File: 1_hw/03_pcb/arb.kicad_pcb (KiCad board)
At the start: 4 copper layers, 100 x 100 mm, 0 parts

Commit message: FEAT: Initial board placement started.
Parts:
- added C1: 1u, Capacitor_SMD:C_0603_1608Metric, F.Cu at (-92.1, 105.8)
- added C10: 2.2u, Capacitor_SMD:C_0603_1608Metric, F.Cu at (-92.1, 128.4)
- added C100: 100n, Capacitor_SMD:C_0603_1608Metric, F.Cu at (126.6, 109.2)
- added C101: 100n, Capacitor_SMD:C_0603_1608Metric, F.Cu at (137.9, 108.7)
- added C102: 100n, Capacitor_SMD:C_0603_1608Metric, F.Cu at (245.0, 110.6)
- added C103: 100n, Capacitor_SMD:C_0603_1608Metric, F.Cu at (252.0, 106.0)
- added C104: 100n, Capacitor_SMD:C_0603_1608Metric, F.Cu at (254.5, 116.7)
- added C105: 5p, Capacitor_SMD:C_0603_1608Metric, F.Cu at (251.0, 131.0)
- added C106: 100n, Capacitor_SMD:C_0603_1608Metric, F.Cu at (269.0, 111.0)
- added C107: 100n, Capacitor_SMD:C_0603_1608Metric, F.Cu at (269.0, 112.5)
- added C108: 5p, Capacitor_SMD:C_0603_1608Metric, F.Cu at (256.0, 128.5)
- added C109: 22p, Capacitor_SMD:C_0603_1608Metric, F.Cu at (225.4, 149.9)
- added C11: 1u, Capacitor_SMD:C_0603_1608Metric, F.Cu at (-92.1, 130.9)
- added C110: 100n, Capacitor_SMD:C_0603_1608Metric, F.Cu at (59.0, 158.4)
- added C111: 100n, Capacitor_SMD:C_0603_1608Metric, F.Cu at (50.0, 163.7)
- added C112: 100n, Capacitor_SMD:C_0603_1608Metric, F.Cu at (75.2, 158.4)
- added C113: 100n, Capacitor_SMD:C_0603_1608Metric, F.Cu at (63.0, 158.4)
- added C12: 1u, Capacitor_SMD:C_0603_1608Metric, F.Cu at (-88.1, 105.8)
- added C13: 2.2u, Capacitor_SMD:C_0603_1608Metric, F.Cu at (-88.1, 108.3)
- added C14: 2.2u, Capacitor_SMD:C_0603_1608Metric, F.Cu at (-88.1, 110.8)
- added C15: 4.7u, Capacitor_SMD:C_0603_1608Metric, F.Cu at (-88.1, 113.3)
- added C16: 100n, Capacitor_SMD:C_0603_1608Metric, F.Cu at (-88.1, 115.8)
- added C17: 10n, Capacitor_SMD:C_0603_1608Metric, F.Cu at (-88.1, 118.3)
- added C18: 4.7n, Capacitor_SMD:C_0603_1608Metric, F.Cu at (-88.1, 120.8)
- added C19: 6.8p, Capacitor_SMD:C_0603_1608Metric, F.Cu at (-88.1, 123.3)
- added C2: 1u, Capacitor_SMD:C_0603_1608Metric, F.Cu at (-92.1, 108.3)
- added C20: 220n, Capacitor_SMD:C_0603_1608Metric, F.Cu at (-88.1, 125.8)
- added C21: 6.8p, Capacitor_SMD:C_0603_1608Metric, F.Cu at (-88.1, 128.4)
- added C22: 4.7u, Capacitor_SMD:C_0603_1608Metric, F.Cu at (-88.1, 130.9)
- added C23: 4.7u, Capacitor_SMD:C_0603_1608Metric, F.Cu at (-84.1, 105.8)
- added C24: 4.7u, Capacitor_SMD:C_0603_1608Metric, F.Cu at (-84.1, 108.3)
- added C25: 4.7u, Capacitor_SMD:C_0603_1608Metric, F.Cu at (-84.1, 110.8)
- added C26: 4.7u, Capacitor_SMD:C_0603_1608Metric, F.Cu at (-84.1, 113.3)
- added C27: 4.7u, Capacitor_SMD:C_0603_1608Metric, F.Cu at (-84.1, 115.8)
- added C28: 100n, Capacitor_SMD:C_0603_1608Metric, F.Cu at (-84.1, 118.3)
- added C29: 4.7u, Capacitor_SMD:C_0603_1608Metric, F.Cu at (-84.1, 120.8)
- added C3: 1u, Capacitor_SMD:C_0603_1608Metric, F.Cu at (-92.1, 110.8)
- added C30: 4.7u, Capacitor_SMD:C_0603_1608Metric, F.Cu at (-84.1, 123.3)
- added C31: 100n, Capacitor_SMD:C_0603_1608Metric, F.Cu at (-84.1, 125.8)
- added C32: 100n, Capacitor_SMD:C_0603_1608Metric, F.Cu at (-84.1, 128.4)
- added C33: 100n, Capacitor_SMD:C_0603_1608Metric, F.Cu at (187.8, 50.0)
- added C34: 100n, Capacitor_SMD:C_0603_1608Metric, F.Cu at (193.9, 88.0)
- added C35: 100n, Capacitor_SMD:C_0603_1608Metric, F.Cu at (186.0, 66.0)
- added C36: 100n, Capacitor_SMD:C_0603_1608Metric, F.Cu at (171.0, 57.5)
- added C37: 5p, Capacitor_SMD:C_0603_1608Metric, F.Cu at (185.5, 71.6)
- added C38: 2.2u, Capacitor_SMD:C_0603_1608Metric, F.Cu at (-35.8, 282.7)
- added C39: 2.2u, Capacitor_SMD:C_0603_1608Metric, F.Cu at (-35.8, 285.2)
- added C4: 10u, Capacitor_SMD:C_0603_1608Metric, F.Cu at (-92.1, 113.3)
- added C40: 100n, Capacitor_SMD:C_0603_1608Metric, F.Cu at (-35.8, 287.7)
- added C41: 100n, Capacitor_SMD:C_0603_1608Metric, F.Cu at (-35.8, 290.2)
- added C42: 10u, Capacitor_SMD:C_0603_1608Metric, F.Cu at (-35.8, 292.7)
- added C43: 15p, Capacitor_SMD:C_0603_1608Metric, F.Cu at (142.5, 76.8)
- added C44: 100n, Capacitor_SMD:C_0603_1608Metric, F.Cu at (-31.8, 282.7)
- added C45: 15p, Capacitor_SMD:C_0603_1608Metric, F.Cu at (142.5, 74.2)
- added C46: 100n, Capacitor_SMD:C_0603_1608Metric, F.Cu at (-31.8, 287.7)
- added C47: 100n, Capacitor_SMD:C_0603_1608Metric, F.Cu at (-31.8, 290.2)
- added C48: 100n, Capacitor_SMD:C_0603_1608Metric, F.Cu at (-31.8, 292.7)
- added C49: 1u, Capacitor_SMD:C_0603_1608Metric, F.Cu at (-31.8, 295.2)
- added C5: 4.7u, Capacitor_SMD:C_0603_1608Metric, F.Cu at (-92.1, 115.8)
- added C50: 100n, Capacitor_SMD:C_0603_1608Metric, F.Cu at (-27.8, 282.7)
- added C51: 100n, Capacitor_SMD:C_0603_1608Metric, F.Cu at (-27.8, 285.2)
- added C52: 100n, Capacitor_SMD:C_0603_1608Metric, F.Cu at (-27.8, 287.7)
- added C53: 1u, Capacitor_SMD:C_0603_1608Metric, F.Cu at (-27.8, 290.2)
- added C54: 100n, Capacitor_SMD:C_0603_1608Metric, F.Cu at (-27.8, 292.7)
- added C55: 100n, Capacitor_SMD:C_0603_1608Metric, F.Cu at (-27.8, 295.2)
- added C56: 100n, Capacitor_SMD:C_0603_1608Metric, F.Cu at (-23.8, 282.7)
- added C57: 100n, Capacitor_SMD:C_0603_1608Metric, F.Cu at (-23.8, 285.2)
- added C58: 100n, Capacitor_SMD:C_0603_1608Metric, F.Cu at (-23.8, 287.7)
- added C59: 100n, Capacitor_SMD:C_0603_1608Metric, F.Cu at (116.0, 103.8)
- added C6: 100n, Capacitor_SMD:C_0603_1608Metric, F.Cu at (-92.1, 118.3)
- added C60: 100n, Capacitor_SMD:C_0603_1608Metric, F.Cu at (108.5, 99.3)
- added C61: 4.7u, Capacitor_SMD:C_0603_1608Metric, F.Cu at (117.5, 103.8)
- added C62: 4.7u, Capacitor_SMD:C_0603_1608Metric, F.Cu at (108.5, 97.8)
- added C63: 4.7u, Capacitor_SMD:C_0603_1608Metric, F.Cu at (108.5, 102.8)
- added C64: 100n, Capacitor_SMD:C_0603_1608Metric, F.Cu at (108.5, 101.3)
- added C65: 100n, Capacitor_SMD:C_0603_1608Metric, F.Cu at (119.0, 92.8)
- added C66: 100n, Capacitor_SMD:C_0603_1608Metric, F.Cu at (116.5, 92.0)
- added C67: 100n, Capacitor_SMD:C_0603_1608Metric, F.Cu at (112.5, 103.8)
- added C68: 4.7u, Capacitor_SMD:C_0603_1608Metric, F.Cu at (119.0, 91.3)
- added C69: 4.7u, Capacitor_SMD:C_0603_1608Metric, F.Cu at (115.0, 92.0)
- added C7: 1u, Capacitor_SMD:C_0603_1608Metric, F.Cu at (-92.1, 120.8)
- added C70: 4.7u, Capacitor_SMD:C_0603_1608Metric, F.Cu at (114.0, 103.8)
- added C71: 100n, Capacitor_SMD:C_0603_1608Metric, F.Cu at (132.1, 58.6)
- added C72: 4.7u, Capacitor_SMD:C_0603_1608Metric, F.Cu at (117.1, 74.3)
- added C73: 27p, Capacitor_SMD:C_0603_1608Metric, F.Cu at (113.1, 70.1)
- added C74: 4.7u, Capacitor_SMD:C_0603_1608Metric, F.Cu at (117.1, 77.8)
- added C75: 27p, Capacitor_SMD:C_0603_1608Metric, F.Cu at (116.4, 67.3)
- added C76: 100n, Capacitor_SMD:C_0603_1608Metric, F.Cu at (118.6, 74.3)
- added C77: 3.3u, Capacitor_SMD:C_0603_1608Metric, F.Cu at (133.6, 69.6)
- added C78: 100n, Capacitor_SMD:C_0603_1608Metric, F.Cu at (118.6, 77.8)
- added C79: 100n, Capacitor_SMD:C_0603_1608Metric, F.Cu at (117.8, 80.1)
- added C8: 2.2u, Capacitor_SMD:C_0603_1608Metric, F.Cu at (-92.1, 123.3)
- added C80: 100n, Capacitor_SMD:C_0603_1608Metric, F.Cu at (136.1, 78.1)
- added C81: 100n, Capacitor_SMD:C_0603_1608Metric, F.Cu at (123.1, 67.6)
- added C82: 100n, Capacitor_SMD:C_0603_1608Metric, F.Cu at (125.4, 84.3)
- added C83: 100n, Capacitor_SMD:C_0603_1608Metric, F.Cu at (131.6, 84.6)
- added C84: 100n, Capacitor_SMD:C_0603_1608Metric, F.Cu at (136.1, 74.6)
- added C85: 100n, Capacitor_SMD:C_0603_1608Metric, F.Cu at (128.1, 67.6)
- added C86: 100n, Capacitor_SMD:C_0603_1608Metric, F.Cu at (155.9, 57.6)
- added C87: 100n, Capacitor_SMD:C_0603_1608Metric, F.Cu at (187.5, 78.4)
- added C88: 100n, Capacitor_SMD:C_0603_1608Metric, F.Cu at (189.5, 104.0)
- added C89: 100n, Capacitor_SMD:C_0603_1608Metric, F.Cu at (189.5, 107.0)
- added C9: 2.2u, Capacitor_SMD:C_0603_1608Metric, F.Cu at (-92.1, 125.8)
- added C90: 100n, Capacitor_SMD:C_0603_1608Metric, F.Cu at (176.0, 107.0)
- added C91: 100n, Capacitor_SMD:C_0603_1608Metric, F.Cu at (116.9, 121.9)
- added C92: 100n, Capacitor_SMD:C_0603_1608Metric, F.Cu at (111.9, 121.9)
- added C93: 100n, Capacitor_SMD:C_0603_1608Metric, F.Cu at (119.4, 121.9)
- added C94: 5p, Capacitor_SMD:C_0603_1608Metric, F.Cu at (131.3, 117.3)
- added C95: 5p, Capacitor_SMD:C_0603_1608Metric, F.Cu at (168.0, 104.7)
- added C96: 100n, Capacitor_SMD:C_0603_1608Metric, F.Cu at (149.6, 115.9)
- added C97: 100n, Capacitor_SMD:C_0603_1608Metric, F.Cu at (148.6, 106.0)
- added C98: 100n, Capacitor_SMD:C_0603_1608Metric, F.Cu at (138.8, 119.9)
- added C99: 100n, Capacitor_SMD:C_0603_1608Metric, F.Cu at (155.6, 101.5)
- added D1: LED, LED_SMD:LED_1206_3216Metric, F.Cu at (-66.1, 120.9)
- added D2: MBRM120ET1G, BRZK_DIODE:D_SMP_DO-216AA, F.Cu at (-66.1, 106.6)
- added D3: MBRM120ET1G, BRZK_DIODE:D_SMP_DO-216AA, F.Cu at (-66.1, 110.8)
- added D4: LED, LED_SMD:LED_1206_3216Metric, F.Cu at (79.0, 94.1)
- added D5: LED, LED_SMD:LED_1206_3216Metric, F.Cu at (83.5, 94.1)
- added D6: LED, LED_SMD:LED_1206_3216Metric, F.Cu at (88.0, 94.1)
- added D7: LED, LED_SMD:LED_1206_3216Metric, F.Cu at (104.0, 76.1)
- added D8: LED, LED_SMD:LED_1206_3216Metric, F.Cu at (108.5, 76.0)
- added D9: BAT54L, Package_TO_SOT_SMD:SOT-23, F.Cu at (260.1, 130.1)
- added FB1: 100@100MHz, Inductor_SMD:L_0603_1608Metric, F.Cu at (187.8, 47.0)
- added FB2: 30@100MHz, Inductor_SMD:L_0603_1608Metric, F.Cu at (193.9, 86.0)
- added H1: MOUNTING HOLE, MountingHole:MountingHole_3.2mm_M3_Pad, F.Cu at (105.7, 48.0)
- added H2: MOUNTING HOLE, MountingHole:MountingHole_3.2mm_M3_Pad, F.Cu at (195.7, 48.0)
- added H3: MOUNTING HOLE, MountingHole:MountingHole_3.2mm_M3_Pad, F.Cu at (105.7, 137.9)
- added H4: MOUNTING HOLE, MountingHole:MountingHole_3.2mm_M3_Pad, F.Cu at (195.7, 137.9)
- added J1: TYPE-C-31-M-12, Connector_USB:USB_C_Receptacle_GCT_USB4105-xx-A_16P_TopMnt_Horizontal, F.Cu at (104.5, 64.0)
- added J2: SMA, BRZK_CONN_COAX:SMA_TH_Horizontal_KH-SMA-K513-G, F.Cu at (196.2, 61.1)
- added J3: SMA, BRZK_CONN_COAX:SMA_TH_Horizontal_KH-SMA-K513-G, F.Cu at (196.2, 70.8)
- added J4: BNC, BRZK_CONN_COAX:BNC_TH_Horizontal_DOSIN-801-0050, F.Cu at (151.8, 136.2)
- added J5: PH-00244, Connector_PinHeader_2.54mm:PinHeader_2x05_P2.54mm_Vertical, F.Cu at (-67.7, 82.3)
- added L1: 4.7u, Inductor_SMD:L_0603_1608Metric, F.Cu at (-84.1, 130.9)
- added L2: 4.7u, Inductor_SMD:L_0603_1608Metric, F.Cu at (-80.1, 105.8)
- added L3: 10u, Inductor_SMD:L_0603_1608Metric, F.Cu at (114.9, 73.6)
- added L4: 10u, Inductor_SMD:L_0603_1608Metric, F.Cu at (114.8, 77.1)
- added R1: 10k, Resistor_SMD:R_0603_1608Metric, F.Cu at (-80.1, 108.3)
- added R10: 84.5k, Resistor_SMD:R_0603_1608Metric, F.Cu at (-80.1, 130.9)
- added R11: 0, Resistor_SMD:R_0603_1608Metric, F.Cu at (-76.1, 105.8)
- added R12: 0, Resistor_SMD:R_0603_1608Metric, F.Cu at (-76.1, 108.3)
- added R13: 104k, Resistor_SMD:R_0603_1608Metric, F.Cu at (-76.1, 110.8)
- added R14: 1.30M, Resistor_SMD:R_0603_1608Metric, F.Cu at (-76.1, 113.3)
- added R15: 0, Resistor_SMD:R_0603_1608Metric, F.Cu at (-76.1, 115.8)
- added R16: 0, Resistor_SMD:R_0603_1608Metric, F.Cu at (-76.1, 118.3)
- added R17: 0, Resistor_SMD:R_0603_1608Metric, F.Cu at (-76.1, 120.8)
- added R18: 0, Resistor_SMD:R_0603_1608Metric, F.Cu at (-76.1, 123.3)
- added R19: 10k, Resistor_SMD:R_0603_1608Metric, F.Cu at (185.2, 49.3)
- added R2: 10k, Resistor_SMD:R_0603_1608Metric, F.Cu at (-80.1, 110.8)
- added R20: 24.9, Resistor_SMD:R_0603_1608Metric, F.Cu at (186.1, 55.5)
- added R21: 10k, Resistor_SMD:R_0603_1608Metric, F.Cu at (192.3, 84.0)
- added R22: 24.9, Resistor_SMD:R_0603_1608Metric, F.Cu at (193.2, 95.0)
- added R23: 10k, Resistor_SMD:R_0603_1608Metric, F.Cu at (184.5, 66.0)
- added R24: 10k, Resistor_SMD:R_0603_1608Metric, F.Cu at (183.0, 60.0)
- added R25: 10k, Resistor_SMD:R_0603_1608Metric, F.Cu at (182.2, 57.5)
- added R26: 100, Resistor_SMD:R_0603_1608Metric, F.Cu at (187.0, 70.0)
- added R27: 100, Resistor_SMD:R_0603_1608Metric, F.Cu at (188.5, 71.6)
- added R28: 24.9, Resistor_SMD:R_0603_1608Metric, F.Cu at (182.2, 56.0)
- added R29: 24.9, Resistor_SMD:R_0603_1608Metric, F.Cu at (173.0, 60.0)
- added R3: 10k, Resistor_SMD:R_0603_1608Metric, F.Cu at (-80.1, 113.3)
- added R30: 0, Resistor_SMD:R_0603_1608Metric, F.Cu at (171.0, 56.0)
- added R31: 10k, Resistor_SMD:R_0603_1608Metric, F.Cu at (-23.8, 290.2)
- added R32: 10k, Resistor_SMD:R_0603_1608Metric, F.Cu at (138.4, 53.1)
- added R33: 10k, Resistor_SMD:R_0603_1608Metric, F.Cu at (126.2, 53.1)
- added R34: 10k, Resistor_SMD:R_0603_1608Metric, F.Cu at (113.8, 87.1)
- added R35: 10k, Resistor_SMD:R_0603_1608Metric, F.Cu at (110.8, 87.1)
- added R36: 10k, Resistor_SMD:R_0603_1608Metric, F.Cu at (103.3, 95.8)
- added R37: 220, Resistor_SMD:R_0603_1608Metric, F.Cu at (79.0, 90.1)
- added R38: 220, Resistor_SMD:R_0603_1608Metric, F.Cu at (83.5, 90.1)
- added R39: 220, Resistor_SMD:R_0603_1608Metric, F.Cu at (88.0, 90.1)
- added R4: 499, Resistor_SMD:R_0603_1608Metric, F.Cu at (-80.1, 115.8)
- added R40: 100, Resistor_SMD:R_0603_1608Metric, F.Cu at (110.1, 104.8)
- added R41: 1k, Resistor_SMD:R_0603_1608Metric, F.Cu at (113.6, 83.1)
- added R42: 10k, Resistor_SMD:R_0603_1608Metric, F.Cu at (122.8, 60.1)
- added R43: 2.05k, Resistor_SMD:R_0603_1608Metric, F.Cu at (123.6, 62.6)
- added R44: 10k, Resistor_SMD:R_0603_1608Metric, F.Cu at (132.1, 60.1)
- added R45: 10k, Resistor_SMD:R_0603_1608Metric, F.Cu at (132.1, 61.6)
- added R46: 12k, Resistor_SMD:R_0603_1608Metric, F.Cu at (119.5, 67.5)
- added R47: 4.7k, Resistor_SMD:R_0603_1608Metric, F.Cu at (116.1, 63.6)
- added R48: 10k, Resistor_SMD:R_0603_1608Metric, F.Cu at (119.1, 63.6)
- added R49: 0, Resistor_SMD:R_0603_1608Metric, F.Cu at (118.6, 84.1)
- added R5: 110k, Resistor_SMD:R_0603_1608Metric, F.Cu at (-80.1, 118.3)
- added R50: 0, Resistor_SMD:R_0603_1608Metric, F.Cu at (121.6, 84.1)
- added R51: 220, Resistor_SMD:R_0603_1608Metric, F.Cu at (104.0, 72.1)
- added R52: 220, Resistor_SMD:R_0603_1608Metric, F.Cu at (108.5, 72.0)
- added R53: 10k, Resistor_SMD:R_0603_1608Metric, F.Cu at (158.5, 61.1)
- added R54: 10k, Resistor_SMD:R_0603_1608Metric, F.Cu at (190.0, 81.5)
- added R55: 10k, Resistor_SMD:R_0603_1608Metric, F.Cu at (146.0, 58.8)
- added R56: 10k, Resistor_SMD:R_0603_1608Metric, F.Cu at (176.0, 79.4)
- added R57: 3.9k, Resistor_SMD:R_0603_1608Metric, F.Cu at (189.5, 102.5)
- added R58: 2k, Resistor_SMD:R_0603_1608Metric, F.Cu at (113.4, 121.9)
- added R59: 10k, Resistor_SMD:R_0603_1608Metric, F.Cu at (117.9, 126.9)
- added R6: 1M, Resistor_SMD:R_0603_1608Metric, F.Cu at (-80.1, 120.8)
- added R60: 24.9, Resistor_SMD:R_0603_1608Metric, F.Cu at (128.8, 118.9)
- added R61: 24.9, Resistor_SMD:R_0603_1608Metric, F.Cu at (172.0, 106.3)
- added R62: 24.9, Resistor_SMD:R_0603_1608Metric, F.Cu at (128.8, 115.8)
- added R63: 24.9, Resistor_SMD:R_0603_1608Metric, F.Cu at (172.0, 103.1)
- added R64: 226, Resistor_SMD:R_0603_1608Metric, F.Cu at (134.3, 118.1)
- added R65: 226, Resistor_SMD:R_0603_1608Metric, F.Cu at (134.3, 116.6)
- added R66: 226, Resistor_SMD:R_0603_1608Metric, F.Cu at (164.3, 105.5)
- added R67: 226, Resistor_SMD:R_0603_1608Metric, F.Cu at (164.3, 104.0)
- added R68: 499, Resistor_SMD:R_0603_1608Metric, F.Cu at (137.8, 115.8)
- added R69: 1k, Resistor_SMD:R_0603_1608Metric, F.Cu at (160.3, 103.0)
- added R7: 0, Resistor_SMD:R_0603_1608Metric, F.Cu at (-80.1, 123.3)
- added R70: 499, Resistor_SMD:R_0603_1608Metric, F.Cu at (144.3, 122.1)
- added R71: 1k, Resistor_SMD:R_0603_1608Metric, F.Cu at (153.8, 99.0)
- added R72: 0, Resistor_SMD:R_0603_1608Metric, F.Cu at (151.9, 117.7)
- added R73: 0, Resistor_SMD:R_0603_1608Metric, F.Cu at (145.0, 104.5)
- added R74: 10k, Resistor_SMD:R_0603_1608Metric, F.Cu at (140.4, 109.5)
- added R75: 4.7k, Resistor_SMD:R_0603_1608Metric, F.Cu at (249.0, 115.5)
- added R76: 4.7k, Resistor_SMD:R_0603_1608Metric, F.Cu at (247.0, 115.5)
- added R77: 0, Resistor_SMD:R_0603_1608Metric, F.Cu at (252.5, 131.0)
- added R78: 124k, Resistor_SMD:R_0603_1608Metric, F.Cu at (256.0, 130.1)
- added R79: 10k, Resistor_SMD:R_0603_1608Metric, F.Cu at (267.1, 115.5)
- added R8: 0, Resistor_SMD:R_0603_1608Metric, F.Cu at (-80.1, 125.8)
- added R80: 0, Resistor_SMD:R_0603_1608Metric, F.Cu at (263.5, 131.0)
- added R81: 50, Resistor_SMD:R_0603_1608Metric, F.Cu at (229.5, 149.1)
- added R82: 499, Resistor_SMD:R_0603_1608Metric, F.Cu at (45.0, 160.4)
- added R83: 499, Resistor_SMD:R_0603_1608Metric, F.Cu at (45.0, 158.7)
- added R84: 499, Resistor_SMD:R_0603_1608Metric, F.Cu at (47.5, 157.9)
- added R85: 499, Resistor_SMD:R_0603_1608Metric, F.Cu at (53.6, 166.9)
- added R86: 0, Resistor_SMD:R_0603_1608Metric, F.Cu at (59.0, 159.9)
- added R87: 10k, Resistor_SMD:R_0603_1608Metric, F.Cu at (62.5, 153.9)
- added R88: 5.1k, Resistor_SMD:R_0603_1608Metric, F.Cu at (-60.8, 81.2)
- added R89: 5.1k, Resistor_SMD:R_0603_1608Metric, F.Cu at (-60.8, 83.7)
- added R9: 976k, Resistor_SMD:R_0603_1608Metric, F.Cu at (-80.1, 128.4)
- added R90: 0, Resistor_SMD:R_0603_1608Metric, F.Cu at (-60.8, 86.2)
- added R91: 0, Resistor_SMD:R_0603_1608Metric, F.Cu at (-60.8, 88.8)
- added R92: 0, Resistor_SMD:R_0603_1608Metric, F.Cu at (-60.8, 91.3)
- added R93: 0, Resistor_SMD:R_0603_1608Metric, F.Cu at (-56.8, 81.2)
- added R94: 0, Resistor_SMD:R_0603_1608Metric, F.Cu at (-56.8, 83.7)
- added R95: 0, Resistor_SMD:R_0603_1608Metric, F.Cu at (-56.8, 86.2)
- added R96: 0, Resistor_SMD:R_0603_1608Metric, F.Cu at (-56.8, 88.8)
- added R97: 0, Resistor_SMD:R_0603_1608Metric, F.Cu at (-56.8, 91.3)
- added SW1: TS-1187A-B-A-B, BRZK_SW:SW_SPST_BUTTON_TS-1187A-B-A-B, F.Cu at (115.2, 48.2)
- added SW2: SS-12D02-VG4, BRZK_SW:SW_TH_Slide_SPDT_Straight_SS-12D02-VG4, F.Cu at (136.5, 48.5)
- added SW3: SS-12D02-VG4, BRZK_SW:SW_TH_Slide_SPDT_Straight_SS-12D02-VG4, F.Cu at (124.2, 48.5)
- added U1: TLV70333DBV, Package_TO_SOT_SMD:SOT-23-5, F.Cu at (-71.5, 106.9)
- added U10: LMK1C1103PWR, Package_SO:TSSOP-8_4.4x3mm_P0.65mm, F.Cu at (176.5, 57.5)
- added U11: STM32F446ZETx, Package_QFP:LQFP-144_20x20mm_P0.5mm, F.Cu at (160.5, 80.0)
- added U12: ICE40UP5K-SG48ITR, Package_DFN_QFN:QFN-48-1EP_7x7mm_P0.5mm_EP5.6x5.6mm, F.Cu at (114.7, 97.7)
- added U13: 93LC56BT-I_OT, Package_TO_SOT_SMD:SOT-23-6, F.Cu at (127.9, 60.0)
- added U14: FT2232HL, Package_QFP:LQFP-64_10x10mm_P0.5mm, F.Cu at (127.5, 76.0)
- added U15: W25Q128JVSIQ, Package_SO:SOIC-8_5.23x5.23mm_P1.27mm, F.Cu at (151.5, 61.6)
- added U16: W25Q128JVSIQ, Package_SO:SOIC-8_5.23x5.23mm_P1.27mm, F.Cu at (183.0, 82.0)
- added U17: AD9850, Package_SO:SSOP-28_5.3x10.2mm_P0.65mm, F.Cu at (183.0, 106.0)
- added U18: AD9744, Package_SO:TSSOP-28_4.4x9.7mm_P0.65mm, F.Cu at (115.5, 116.5)
- added U19: LM6171, Package_SO:SOIC-8_3.9x4.9mm_P1.27mm, F.Cu at (144.3, 117.1)
- added U2: TLV76133DCY, Package_TO_SOT_SMD:SOT-223-3_TabPin2, F.Cu at (-69.1, 131.8)
- added U20: LM6171, Package_SO:SOIC-8_3.9x4.9mm_P1.27mm, F.Cu at (153.8, 105.0)
- added U21: TMUX6104, Package_SO:TSSOP-14_4.4x5mm_P0.65mm, F.Cu at (132.5, 108.0)
- added U22: TPL0401B-10, Package_TO_SOT_SMD:Texas_R-PDSO-G6, F.Cu at (248.1, 111.8)
- added U23: THS3491, Package_SO:Texas_R-PDSO-G8_EP2.95x4.9mm_Mask2.4x3.1mm, F.Cu at (254.0, 111.4)
- added U24: ADG1219BRJZ, Package_TO_SOT_SMD:SOT-23-8, F.Cu at (265.1, 112.0)
- added U25: LM6171, Package_SO:SOIC-8_3.9x4.9mm_P1.27mm, F.Cu at (53.5, 159.4)
- added U26: TMUX6104, Package_SO:TSSOP-14_4.4x5mm_P0.65mm, F.Cu at (69.5, 158.9)
- added U3: TLV70333DBV, Package_TO_SOT_SMD:SOT-23-5, F.Cu at (-71.5, 111.5)
- added U4: LM3880MF-1AA, Package_TO_SOT_SMD:SOT-23-6, F.Cu at (-71.5, 116.2)
- added U5: TLV70312DBV, Package_TO_SOT_SMD:SOT-23-5, F.Cu at (-71.5, 120.8)
- added U6: TLV70325DBV, Package_TO_SOT_SMD:SOT-23-5, F.Cu at (-71.5, 125.4)
- added U7: TPS65131RGE, Package_DFN_QFN:VQFN-24-1EP_4x4mm_P0.5mm_EP2.45x2.45mm, F.Cu at (-65.8, 116.0)
- added U8: TPD2E001DRL, Package_TO_SOT_SMD:SOT-553, F.Cu at (-67.2, 124.3)
- added U9: ADG1219BRJZ, Package_TO_SOT_SMD:SOT-23-8, F.Cu at (186.5, 62.0)
- added X1: ASE-10.000MHz, Oscillator:Oscillator_SMD_Abracon_ASE-4Pin_3.2x2.5mm, F.Cu at (185.3, 52.0)
- added X2: ASE-100.000MHz, Oscillator:Oscillator_SMD_Abracon_ASE-4Pin_3.2x2.5mm, F.Cu at (192.3, 91.0)
- added Y1: 32.768k, Crystal:Crystal_SMD_3215-2Pin_3.2x1.5mm, F.Cu at (145.5, 75.5)
- added Y2: 12 MHz, Crystal:Crystal_SMD_3225-4Pin_3.2x2.5mm, F.Cu at (113.3, 67.4)
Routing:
- added copper zone on In1.Cu, net GND
- added copper zone on In2.Cu, net GND

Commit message: FEAT: Finished placement of components, switches, etc.
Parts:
- moved C55 302.2 mm to (172.0, 68.5), turned to 90 degrees
- moved C39 299.3 mm to (173.8, 71.5)
- moved C53 294.3 mm to (173.8, 75.8)
- moved C54 290.9 mm to (173.8, 83.0)
- moved C51 289.6 mm to (173.8, 77.2)
- moved C42 288.9 mm to (147.7, 69.5), turned to 180 degrees
- moved C56 285.8 mm to (163.5, 66.7), turned to 90 degrees
- moved C57 284.2 mm to (158.0, 66.7), turned to 90 degrees
- moved R31 283.9 mm to (151.0, 66.5)
- moved C40 282.6 mm to (148.0, 73.0), turned to 90 degrees
- moved C52 280.0 mm to (172.0, 91.5)
- moved C58 279.7 mm to (149.4, 68.0), turned to 180 degrees
- moved C41 279.5 mm to (147.2, 79.0), turned to 180 degrees
- moved C38 278.6 mm to (168.5, 93.3), turned to -90 degrees
- moved C48 276.4 mm to (159.5, 93.3), turned to -90 degrees
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
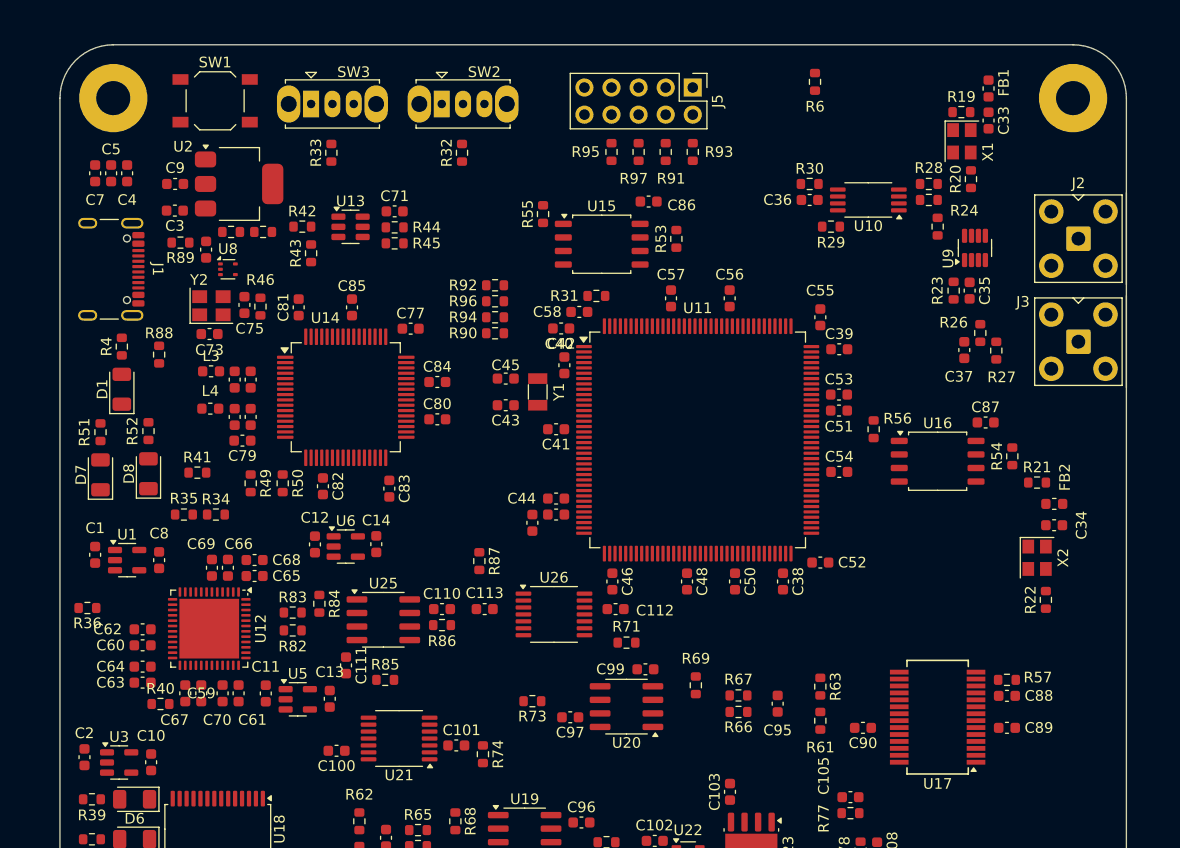
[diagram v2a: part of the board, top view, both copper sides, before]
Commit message: MINOR: Started laying out signal tracks. About 1/4th of the way done. Started on Digital, 3P3V Power, Clocking.
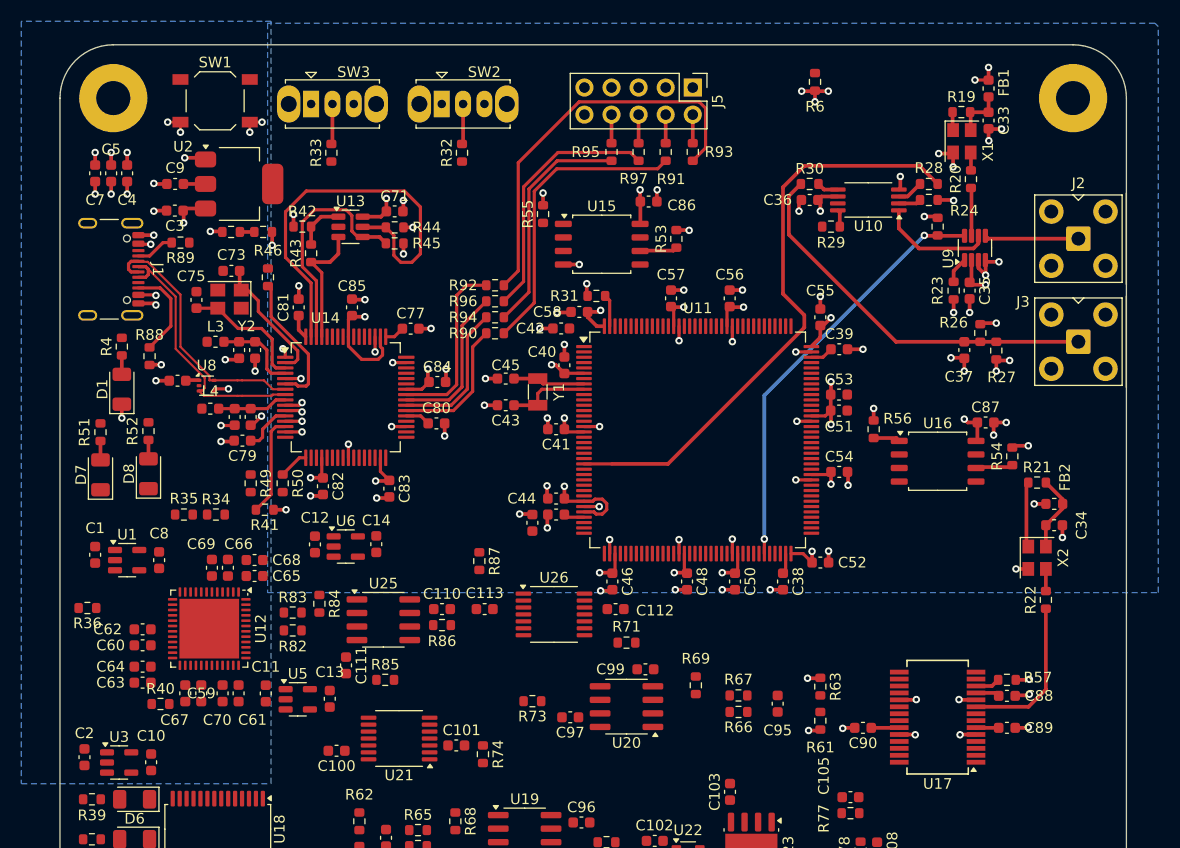
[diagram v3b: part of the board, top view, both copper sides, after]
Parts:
- moved C28 12.6 mm to (111.7, 74.5), turned to 180 degrees
- moved U8 11.1 mm to (114.4, 74.9)
- moved R41 7.21 mm to (119.9, 86.5), turned to 180 degrees
- moved C73 6.26 mm to (116.8, 64.2), turned to 180 degrees
- moved C75 4.52 mm to (113.5, 66.9), turned to 90 degrees
- moved R46 2.84 mm to (120.2, 64.8)
- moved C72 2.80 mm to (117.5, 71.6)
- moved C76 2.80 mm to (119.0, 71.6)
- moved L3 2.80 mm to (115.3, 70.8)
- moved Y2 1.81 mm to (116.6, 66.8), turned to 180 degrees
- moved R88 0.91 mm to (109.1, 72.2)
- moved C80 0.39 mm to (136.0, 78.5)
- turned R91 to 90 degrees
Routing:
- net GND: track 0.00 -> 132.7 mm, vias 0 -> 102
- net 3P3V_D: track 0.00 -> 113.1 mm, vias 0 -> 38
- net CLK_10MHZ_DIST_MCU_3P3: track 0.00 -> 56.0 mm
- net GPIO_SW-SEL_MCU_CLKMUX_3P3: track 0.00 -> 39.8 mm, vias 0 -> 2
- net Net-(U13-CS): track 0.00 -> 39.4 mm
- net JTAG_MCU_TMS_3P3: track 0.00 -> 37.7 mm
- net CLK_10MHZ_DIST_EXT_3P3: track 0.00 -> 36.5 mm
- net JTAG_MCU_TCK_3P3: track 0.00 -> 28.0 mm
- net USB_DATA_CONN_FTDI_P: track 0.00 -> 25.9 mm
- net USB_DATA_CONN_FTDI_N: track 0.00 -> 24.4 mm
- net JTAG_MCU_TDO_3P3: track 0.00 -> 23.9 mm
- net JTAG_MCU_TDI_3P3: track 0.00 -> 21.8 mm
- net Net-(U13-CLK): track 0.00 -> 21.8 mm
- net JTAG_FTDI_TMS_3P3: track 0.00 -> 16.7 mm
- net CLK_100MHZ_DDS_3P3: track 0.00 -> 14.8 mm
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- added copper zone on B.Cu, net 3P3V_D
- added copper zone on B.Cu, net 5P0V

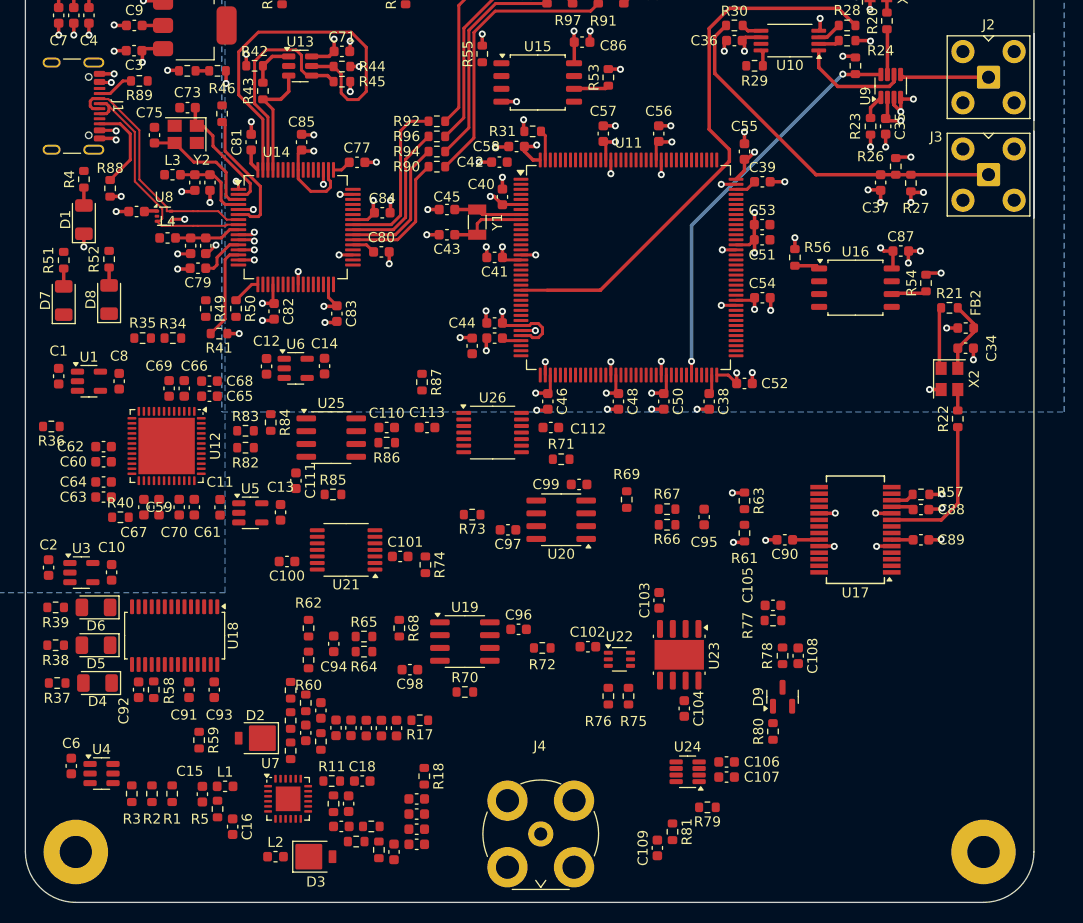
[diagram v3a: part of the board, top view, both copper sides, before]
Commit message: FEAT: Changed Inductor to higher current. Continued layout. Assigned some Netclasses.
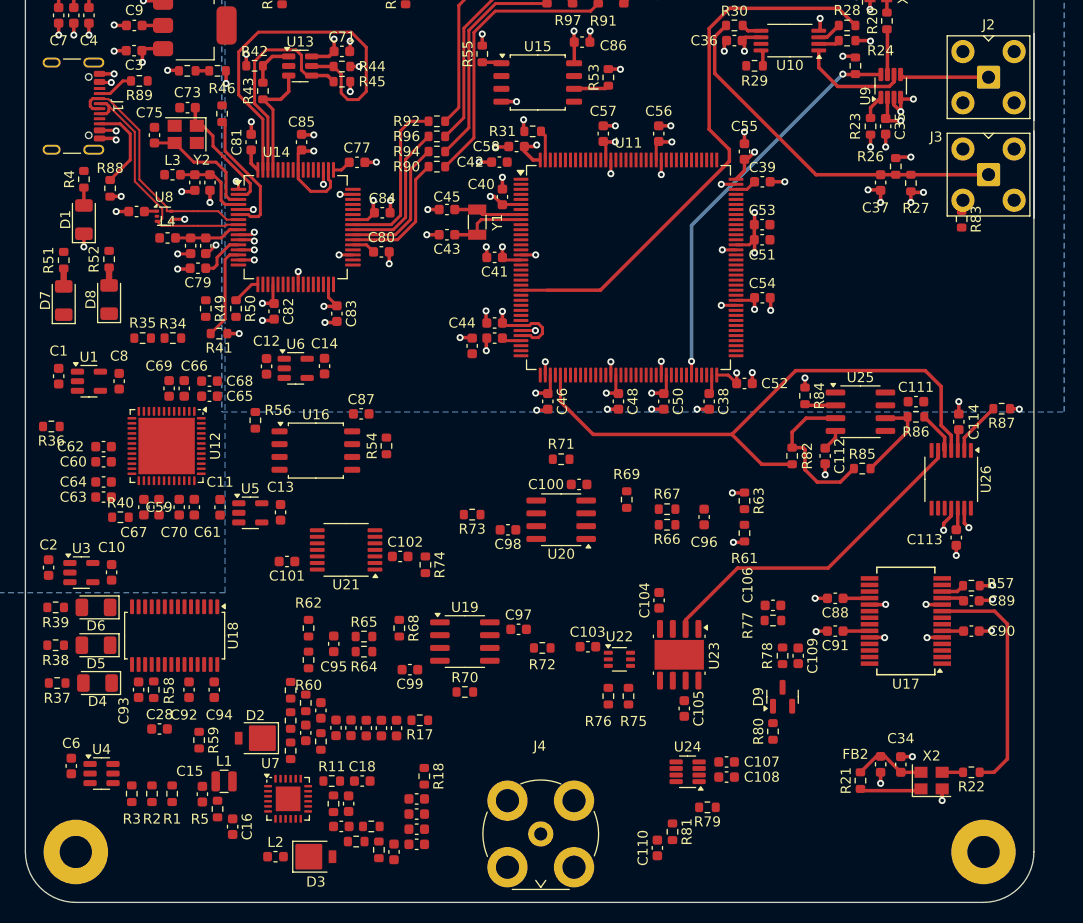
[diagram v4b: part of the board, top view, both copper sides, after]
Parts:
- added C28: 100n, Capacitor_SMD:C_0603_1608Metric, F.Cu at (114.0, 125.8)
- added C88: 100n, Capacitor_SMD:C_0603_1608Metric, F.Cu at (181.0, 112.8)
- L1: footprint Inductor_SMD:L_0603_1608Metric -> BRZK_INDUCTOR:L_SMD_L2.5_W2.0_Metric
- moved R83 74.0 mm to (193.5, 75.2), turned to -90 degrees
- moved R87 57.5 mm to (197.5, 94.0), turned to 180 degrees
- moved C87 55.9 mm to (134.0, 94.5)
- moved R56 55.9 mm to (123.5, 95.2)
- moved U16 55.9 mm to (129.5, 98.2)
- moved R54 55.9 mm to (136.5, 97.7)
- moved R82 54.2 mm to (176.7, 98.7), turned to 90 degrees
- moved R84 53.0 mm to (178.0, 92.7)
- moved C114 52.7 mm to (193.2, 95.3), turned to 90 degrees
- moved R85 52.5 mm to (183.7, 99.9)
- moved C111 52.5 mm to (189.0, 93.3)
- moved R86 52.5 mm to (189.0, 94.8)
- moved U25 52.5 mm to (183.5, 94.3)
- moved C112 52.5 mm to (180.0, 98.7)
- moved R21 47.7 mm to (183.5, 130.9), turned to 90 degrees
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- renumbered C99 to C100, C100 to C101, C101 to C102, C102 to C103, C103 to C104, C104 to C105, C105 to C106, C106 to C107, C107 to C108, C108 to C109, C109 to C110, C110 to C111, C111 to C112, C112 to C113, C113 to C114, C88 to C89, C89 to C90, C90 to C91, C91 to C92, C92 to C93, C93 to C94, C94 to C95, C95 to C96, C96 to C97, C97 to C98, C98 to C99
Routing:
- net ANALOG_DAC2_MCU_AMUX3: track 0.00 -> 59.0 mm
- net ANALOG_DC-OFFSET_AMUX3_AMP3: track 0.00 -> 33.3 mm
- net Net-(U25-+): track 0.00 -> 15.7 mm
- net Net-(R85-Pad2): track 0.00 -> 8.91 mm
- net CLK_100MHZ_DDS_3P3: track 14.8 -> 23.7 mm
- net GND: track 132.7 -> 141.3 mm, vias 102 -> 108
- net 3P3V_D: track 113.1 -> 107.2 mm, vias 38 -> 35
- net GPIO_EN_MCU_AMUX3_3P3: track 0.00 -> 5.33 mm
- net Net-(U26-S2): track 0.00 -> 4.92 mm
- net N15P0V_A: track 0.00 -> 4.23 mm
- net SPI_SCLK_MCU_FPGA_3P3: track 3.51 -> 0.00 mm
- net Net-(U25--): track 0.00 -> 3.07 mm
- net 3P3V_A: track 4.18 -> 6.82 mm
- net SPI_CS_MCU_FLASH_3P3_L: track 2.51 -> 0.00 mm
- net 15P0V_A: track 0.00 -> 2.20 mm
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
